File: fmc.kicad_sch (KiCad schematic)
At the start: 6 parts

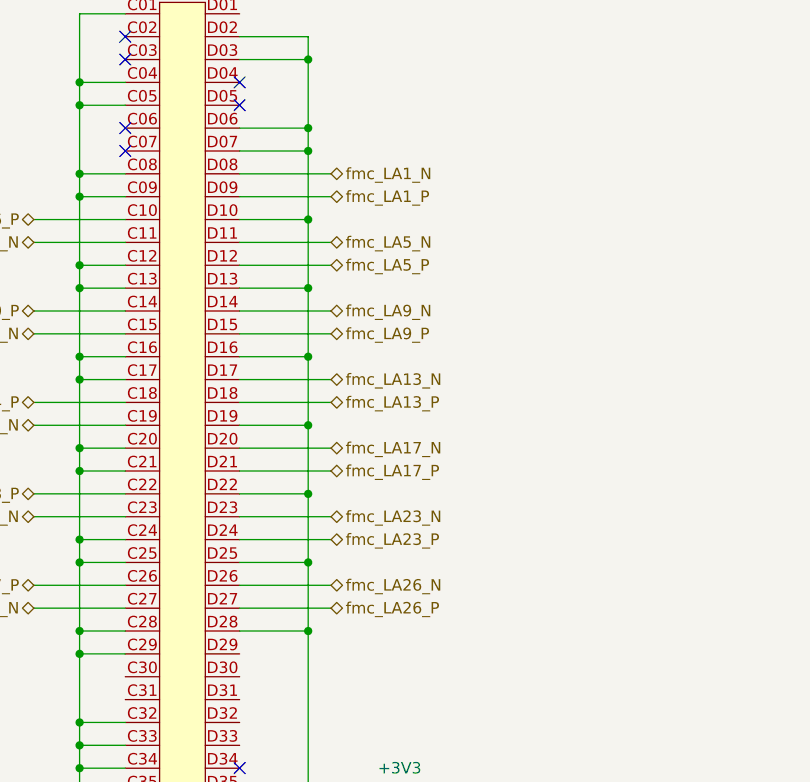
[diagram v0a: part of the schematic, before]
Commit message: Fixed wrong FMC pin labels
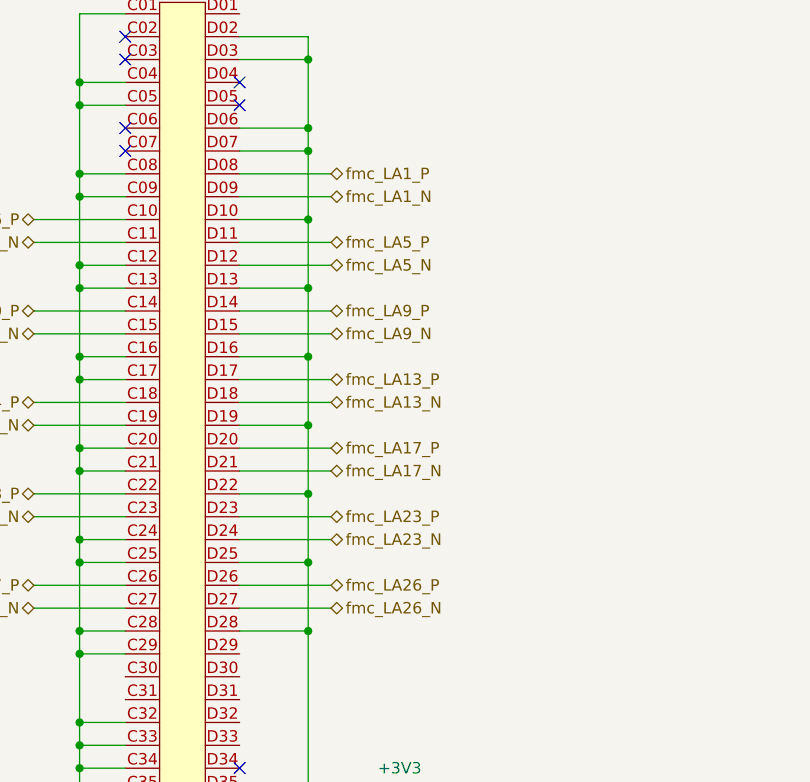
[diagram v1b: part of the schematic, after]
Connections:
- net fmc_LA13_N: now also J1.D18; no longer J1.D17
- net fmc_LA13_P: now also J1.D17; no longer J1.D18
- net fmc_LA17_N: now also J1.D21; no longer J1.D20
- net fmc_LA17_P: now also J1.D20; no longer J1.D21
- net fmc_LA1_N: now also J1.D09; no longer J1.D08
- net fmc_LA1_P: now also J1.D08; no longer J1.D09
- net fmc_LA23_N: now also J1.D24; no longer J1.D23
- net fmc_LA23_P: now also J1.D23; no longer J1.D24
- net fmc_LA26_N: now also J1.D27; no longer J1.D26
- net fmc_LA26_P: now also J1.D26; no longer J1.D27
- net fmc_LA5_N: now also J1.D12; no longer J1.D11
- net fmc_LA5_P: now also J1.D11; no longer J1.D12
- net fmc_LA9_N: now also J1.D15; no longer J1.D14
- net fmc_LA9_P: now also J1.D14; no longer J1.D15
